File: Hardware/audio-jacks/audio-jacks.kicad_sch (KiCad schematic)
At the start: 30 parts, among them J1 Barrel_Jack_Switch, J2 BM28B0.6-24DS/2, J3 AudioJack2_SwitchT, J4 AudioJack2_SwitchT, J5 Conn_01x12_MountingPin, U1 TLV76750DRVx, U2 OPA365xxDBV, U3 TLV76733DRVx

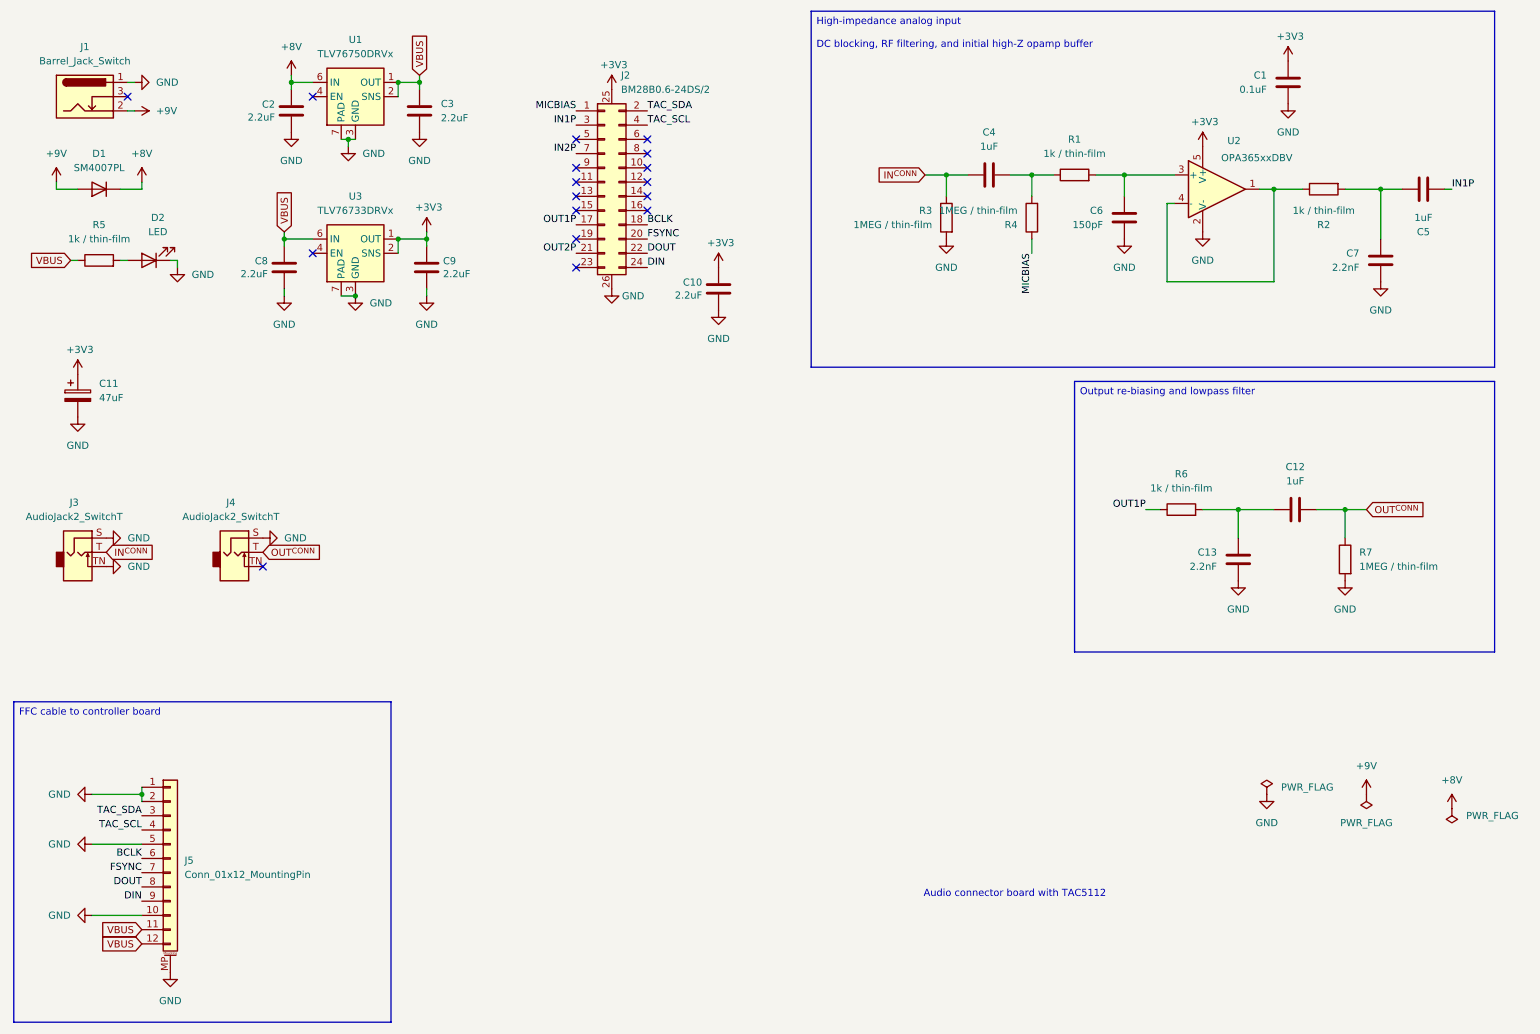
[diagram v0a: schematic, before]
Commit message: Update the audio-jacks board
The old audio jack board actually works quite well, and I've used the
same board now in a few different form factors, which is a good sign.

However, I do want to try doing a stereo board, and the old one was
using mono audio jacks.  That was partly historical, but also partly a
size issue: the particular mono jacks I use are just smaller than the
stereo jacks I have.  And there are obviously fewer components in the
mono setup.

However, exactly because the form factor has worked fairly well, I felt
like I could avoid the whole separate TAC5112 board that I had used with
the (quite nice and compact, but a bit of a pain to route out of) BM28
connector.

The TAC5112 is actually easier to route on its own than using the codec
board - the advantage of that separate board was that I could then do
various test variations using it, and re-use the CODEC board when those
variations failed.  Which they certainly have done - I've tried a lot of
different form factors.

So now that I feel more comfortable with the form factor and think it
works, I might as well put the codec chip directly on the board, which
makes things easier and more compact.

As a result it's not a problem to fit the larger dual op-amp for
buffering the input signal, and the other extra analog components.

There are a few other changes than just switching to stereo jacks and a
dual op-amp.  The big one is that this uses the TAC5242 instead of the
TAC5112.  It doesn't do i2c for control, it's set up with hardware
strapping of five control pins instead.  I liked having i2c for testing
things, but again, now I basically know what my setup is.

The FFC cable still brings in i2c from the controller board, but now
it's only connected to the EEPROM.  And since that's the only thing it
is used for, I decided to upgrade it a bit - from a 2kbit EEPROM to a
64kbit one.

The 2kbit one worked fine, but I didn't expect to have as much config
data as I do.  For all the best kinds of reasons: t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
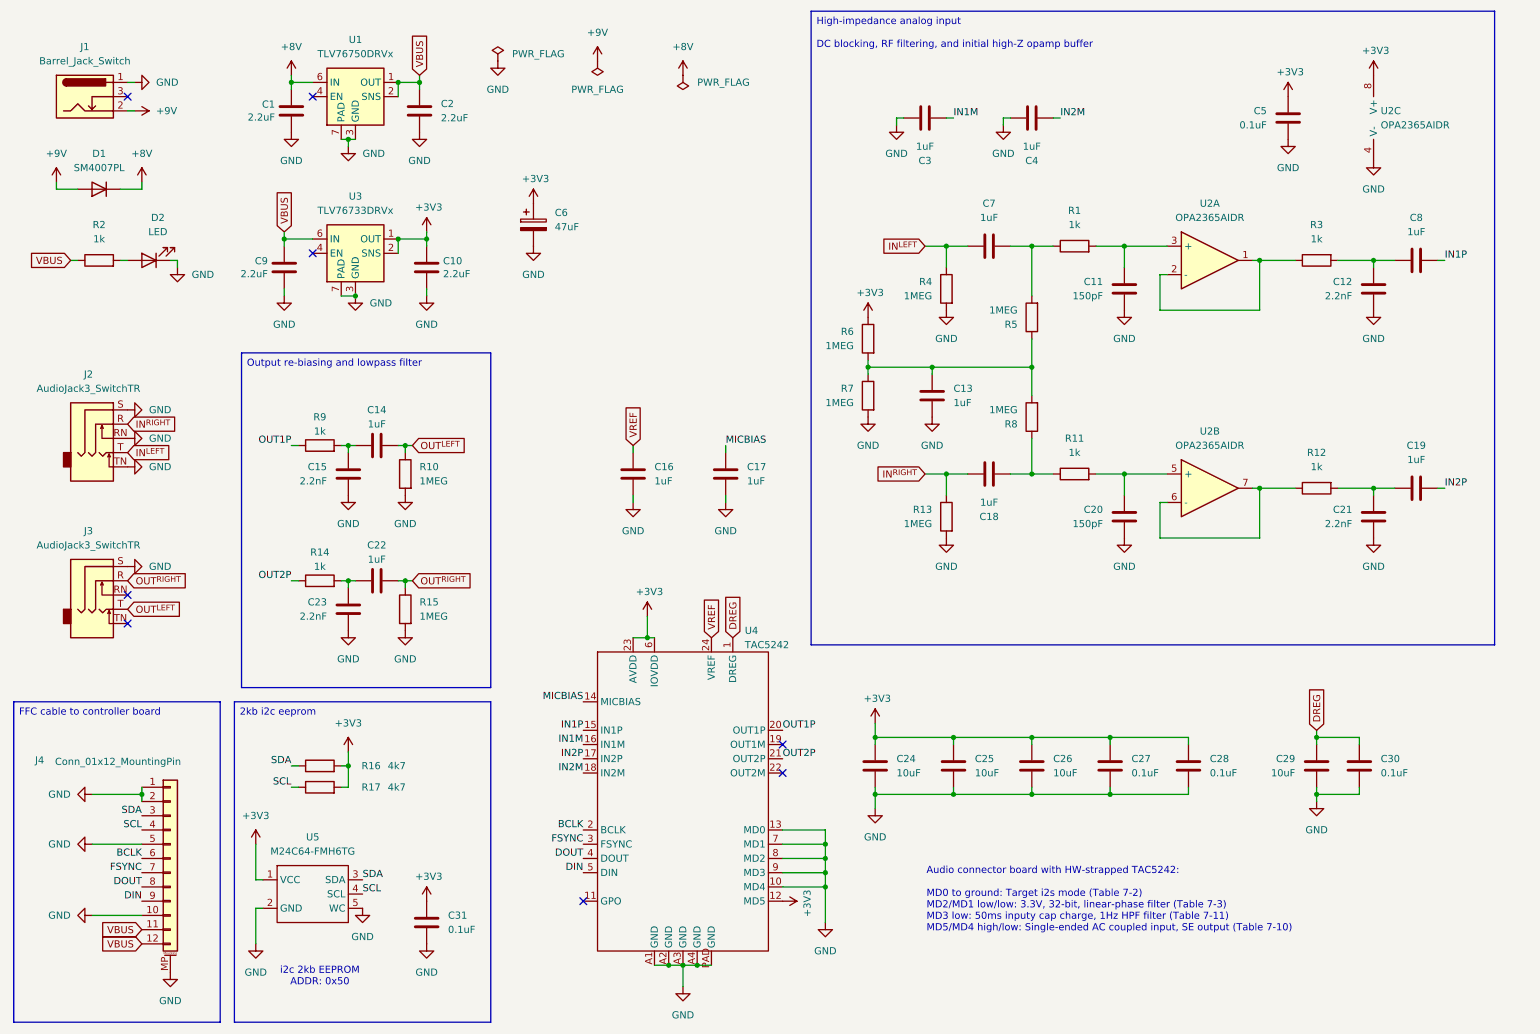
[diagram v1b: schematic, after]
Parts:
- removed C10: 2.2uF, Capacitor_SMD:C_0805_2012Metric, symbol Device:C
- removed J2: BM28B0.6-24DS/2, Mylib:BM28B0.6-24DS, symbol Mylib:BM28B0.6-24DS
- removed J3, J4: AudioJack2_SwitchT, Mylib:CK-6.35-no-NPTH, symbol Connector_Audio:AudioJack2_SwitchT
- removed U2: OPA365xxDBV, Package_TO_SOT_SMD:SOT-23-5, symbol Amplifier_Operational:OPA365xxDBV
- added C13, C16, C17, C18, C19, C22, C3, C4: 1uF, Capacitor_SMD:C_0603_1608Metric, symbol Device:C
- added C20: 150pF, Capacitor_SMD:C_0402_1005Metric, symbol Device:C
- added C21, C23: 2.2nF, Capacitor_SMD:C_0402_1005Metric, symbol Device:C
- added C24, C25, C26, C29: 10uF, Capacitor_SMD:C_0603_1608Metric, symbol Device:C
- added C27, C28, C30, C31: 0.1uF, Capacitor_SMD:C_0402_1005Metric, symbol Device:C
- added J2, J3: AudioJack3_SwitchTR, Mylib:NRJ6HM-1-PRE, symbol Connector_Audio:AudioJack3_SwitchTR
- added R11, R12, R14: 1k, Resistor_SMD:R_0402_1005Metric, symbol Device:R
- added R13, R15, R6, R7, R8: 1MEG, Resistor_SMD:R_0402_1005Metric, symbol Device:R
- added R16, R17: 4k7, Resistor_SMD:R_0402_1005Metric, symbol Device:R
- added U2: OPA2365AIDR, Package_SO:SOIC-8_3.9x4.9mm_P1.27mm, symbol Device:Opamp_Dual
- added U4: TAC5242, Mylib:TAC5242, symbol Mylib:TAC5242
- added U5: M24C64-FMH6TG, Mylib:UFDFPN5, symbol Mylib:M24C02-FMH
- C14: renamed from C12; LCSC PN C519560 -> C85862
- C7: renamed from C4; LCSC PN C519560 -> C85862
- C8: renamed from C5; LCSC PN C519560 -> C85862
- R1: value 1k / thin-film -> 1k
- R10: renamed from R7; value 1MEG / thin-film -> 1MEG
- R2: renamed from R5; value 1k / thin-film -> 1k
- R3: renamed from R2; value 1k / thin-film -> 1k
- R4: renamed from R3; value 1MEG / thin-film -> 1MEG
- R5: renamed from R4; value 1MEG / thin-film -> 1MEG
- R9: renamed from R6; value 1k / thin-film -> 1k
- renumbered C2 to C1, C9 to C10, C6 to C11, C7 to C12, C13 to C15, C3 to C2, C1 to C5, C11 to C6, C8 to C9, J5 to J4
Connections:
- net +3V3: now also C24.1, C25.1, C26.1, C27.1, C28.1, C31.1, R16.2, R17.2, R6.1, U2.8 (V+), U4.12 (MD5), U4.23 (AVDD), U4.6 (IOVDD), U5.1 (VCC)
- net BCLK: now also U4.2 (BCLK)
- net DIN: now also U4.5 (DIN)
- net DOUT: now also U4.4 (DOUT)
- net FSYNC: now also U4.3 (FSYNC)
- net GND: now also C13.1, C16.2, C17.2, C20.2, C21.1, C23.1, C24.2, C25.2, C26.2, C27.2, C28.2, C29.2, C3.1, C30.2, C31.2, C4.1, J2.RN, J2.S, J2.TN, J3.S, R13.2, R15.2, R7.2, U2.4 (V-), U4.10 (MD4), U4.13 (MD0), U4.7 (MD1), U4.8 (MD2), U4.9 (MD3), U4.A1 (GND), U4.A2 (GND), U4.A3 (GND), U4.A4 (GND), U4.PAD (GND), U5.2 (GND), U5.5 (WC)
- net IN1P: now also U4.15 (IN1P)
- net IN2P: now also C19.2, U4.17 (IN2P)
- net MICBIAS: now also C17.1, U4.14 (MICBIAS); no longer R5.1
- net OUT1P: now also U4.20 (OUT1P)
- net OUT2P: now also R14.1, U4.21 (OUT2P)
- net at R3.1: now also U2.1, U2.2 (-)
- net at C11.1, R1.2: now also U2.3 (+)
- net IN^{CONN} renamed IN^{LEFT}
- net IN^{LEFT}: now also J2.T
- net OUT^{CONN} renamed OUT^{LEFT}
- net OUT^{LEFT}: now also J3.T
- net TAC_SCL renamed SCL
- net SCL: now also R17.1, U5.4 (SCL)
- net TAC_SDA renamed SDA
- net SDA: now also R16.1, U5.3 (SDA)
- new net: C13.2, R5.1, R6.2, R7.1, R8.2
- new net: C20.1, R11.2, U2.5 (+)
- new net: R12.1, U2.6 (-), U2.7
- new net: C19.1, C21.2, R12.2
- new net: C22.1, C23.2, R14.2
- new net: C18.2, R11.1, R8.1
- new net DREG: C29.1, C30.1, U4.1 (DREG)
- new net IN1M: C3.2, U4.16 (IN1M)
- new net IN2M: C4.2, U4.18 (IN2M)
- new net IN^{RIGHT}: C18.1, J2.R, R13.1
- new net OUT^{RIGHT}: C22.2, J3.R, R15.1
- new net VREF: C16.1, U4.24 (VREF)
- no-connect marks 17 -> 8
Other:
- note added: "Audio connector board with HW-strapped TAC5242: MD0 to ground: Target i2s mode (Table 7-2) MD2/MD1 low/low: 3.3V, 32-bit, linear-phase filter (Table 7-3) MD3 low: 50ms inputy cap charge, 1Hz HPF filter (Table 7-11) MD5/MD4 high/low: Single-ended AC coupled input, SE output (Table 7-10)"
- note added: "i2c 2kb EEPROM ADDR: 0x50"
- note removed: "Audio connector board with TAC5112"
- moved on the sheet: C11, C12, C14, C15, C5, C6, C7, C8, R1, R10, R3, R4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
